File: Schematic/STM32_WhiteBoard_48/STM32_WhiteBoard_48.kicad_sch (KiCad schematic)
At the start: 41 parts, among them J1 SWDIO+Serial, J2 USB_B_Micro, J3 Header2, J4 Header1, SW1 BOOT0, SW2 RESET, U2 STM32F103CBTx, U3 LD3985M33R_SOT23, U3 W25Q32JVSSIQ, Y1 XC32M4-8.000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

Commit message: Minor layout changes
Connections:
- net PA10: now also J3.3 (Pin_3); no longer J3.4 (Pin_4)
- net PA11: now also J3.2 (Pin_2); no longer J3.3 (Pin_3)
- net PA12: now also J3.1 (Pin_1); no longer J3.2 (Pin_2)
- net PA15: now also J3.6 (Pin_6); no longer J3.1 (Pin_1)
- net PA8: now also J3.5 (Pin_5); no longer J3.6 (Pin_6)
- net PA9: now also J3.4 (Pin_4); no longer J3.5 (Pin_5)
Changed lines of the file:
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@@
     )
   )
-  (global_label "PA15" (shape bidirectional) (at 191.135 108.585 180) (fields_autoplaced)
-    (effects (font (size 1.27 1.27)) (justify right))
-    (property "Intersheetrefs" "${INTERSHEET_REFS}" (at 183.0739 108.585 0)
+  (global_label "PA15" (shape bidirectional) (at 191.135 121.285 180) (fields_autoplaced)
+    (effects (font (size 1.27 1.27)) (justify right))
+    (property "Intersheetrefs" "${INTERSHEET_REFS}" (at 183.0739 121.285 0)
       (effects (font (size 1.27 1.27)) (justify right) hide)
     )
@@
     )
   )
-  (global_label "PA8" (shape bidirectional) (at 191.135 121.285 180) (fields_autoplaced)
-    (effects (font (size 1.27 1.27)) (justify right))
-    (property "Intersheetrefs" "${INTERSHEET_REFS}" (at 184.2834 121.285 0)
+  (global_label "PA8" (shape bidirectional) (at 191.135 118.745 180) (fields_autoplaced)
+    (effects (font (size 1.27 1.27)) (justify right))
+    (property "Intersheetrefs" "${INTERSHEET_REFS}" (at 184.2834 118.745 0)
       (effects (font (size 1.27 1.27)) (justify right) hide)
     )
@@
     )
   )
-  (global_label "PA11" (shape bidirectional) (at 191.135 113.665 180) (fields_autoplaced)
-    (effects (font (size 1.27 1.27)) (justify right))
-    (property "Intersheetrefs" "${INTERSHEET_REFS}" (at 183.0739 113.665 0)
+  (global_label "PA11" (shape bidirectional) (at 191.135 111.125 180) (fields_autoplaced)
+    (effects (font (size 1.27 1.27)) (justify right))
+    (property "Intersheetrefs" "${INTERSHEET_REFS}" (at 183.0739 111.125 0)
       (effects (font (size 1.27 1.27)) (justify right) hide)
     )
@@
     )
   )
-  (global_label "PA12" (shape bidirectional) (at 191.135 111.125 180) (fields_autoplaced)
-    (effects (font (size 1.27 1.27)) (justify right))
-    (property "Intersheetrefs" "${INTERSHEET_REFS}" (at 183.0739 111.125 0)
+  (global_label "PA12" (shape bidirectional) (at 191.135 108.585 180) (fields_autoplaced)
+    (effects (font (size 1.27 1.27)) (justify right))
+    (property "Intersheetrefs" "${INTERSHEET_REFS}" (at 183.0739 108.585 0)
       (effects (font (size 1.27 1.27)) (justify right) hide)
     )
@@
     )
   )
-  (global_label "PA10" (shape bidirectional) (at 191.135 116.205 180) (fields_autoplaced)
-    (effects (font (size 1.27 1.27)) (justify right))
-    (property "Intersheetrefs" "${INTERSHEET_REFS}" (at 183.0739 116.205 0)
+  (global_label "PA10" (shape bidirectional) (at 191.135 113.665 180) (fields_autoplaced)
+    (effects (font (size 1.27 1.27)) (justify right))
+    (property "Intersheetrefs" "${INTERSHEET_REFS}" (at 183.0739 113.665 0)
       (effects (font (size 1.27 1.27)) (justify right) hide)
     )
@@
     )
   )
-  (global_label "PA9" (shape bidirectional) (at 191.135 118.745 180) (fields_autoplaced)
-    (effects (font (size 1.27 1.27)) (justify right))
-    (property "Intersheetrefs" "${INTERSHEET_REFS}" (at 184.2834 118.745 0)
+  (global_label "PA9" (shape bidirectional) (at 191.135 116.205 180) (fields_autoplaced)
+    (effects (font (size 1.27 1.27)) (justify right))
+    (property "Intersheetrefs" "${INTERSHEET_REFS}" (at 184.2834 116.205 0)
       (effects (font (size 1.27 1.27)) (justify right) hide)
     )
@@
         )
       )
+    )
+  )
+  (symbol (lib_id "power:PWR_FLAG") (at 53.975 165.1 0) (unit 1)
+    (in_bom yes) (on_board yes) (dnp no) (fields_autoplaced)
+    (property "Reference" "#FLG05" (at 53.975 163.195 0)
+      (effects (font (size 1.27 1.27)) hide)
+    )
+    (property "Value" "PWR_FLAG" (at 53.975 160.655 0)
+      (effects (font (size 1.27 1.27)) hide)
+    )
+    (property "Footprint" "" (at 53.975 165.1 0)
+      (effects (font (size 1.27 1.27)) hide)
+    )
+    (property "Datasheet" "~" (at 53.975 165.1 0)
+      (effects (font (size 1.27 1.27)) hide)
+    )
+    (pin "1")
+    (instances
+      (project "STM32_WhiteBoard_64"
+        (path "/b9086175-f44c-4e71-b882-25cd78abf8b0"
+          (reference "#FLG05") (unit 1)
+        )
+      )
+      (project "STM32_WhiteBoard_48"
+        (path "/e667a7e9-e434-40bf-934b-fbf6b9624752"
+          (reference "#FLG04") (unit 1)
+        )
+      )

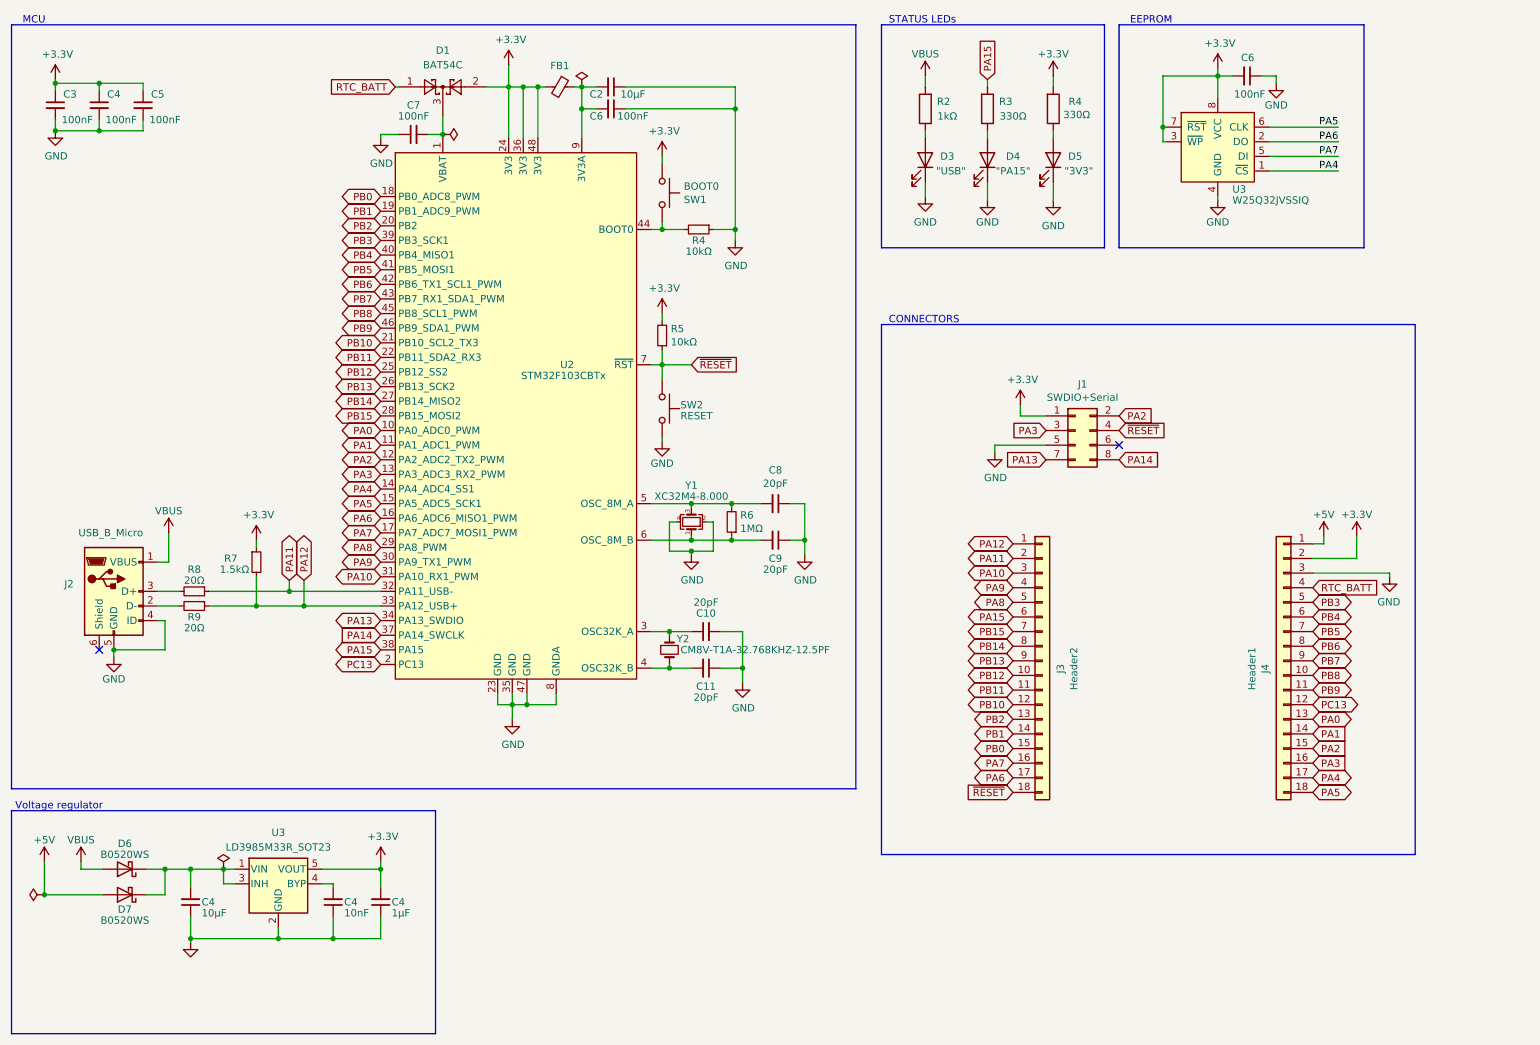
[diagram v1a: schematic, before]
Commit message: Added ESD protection for USB.
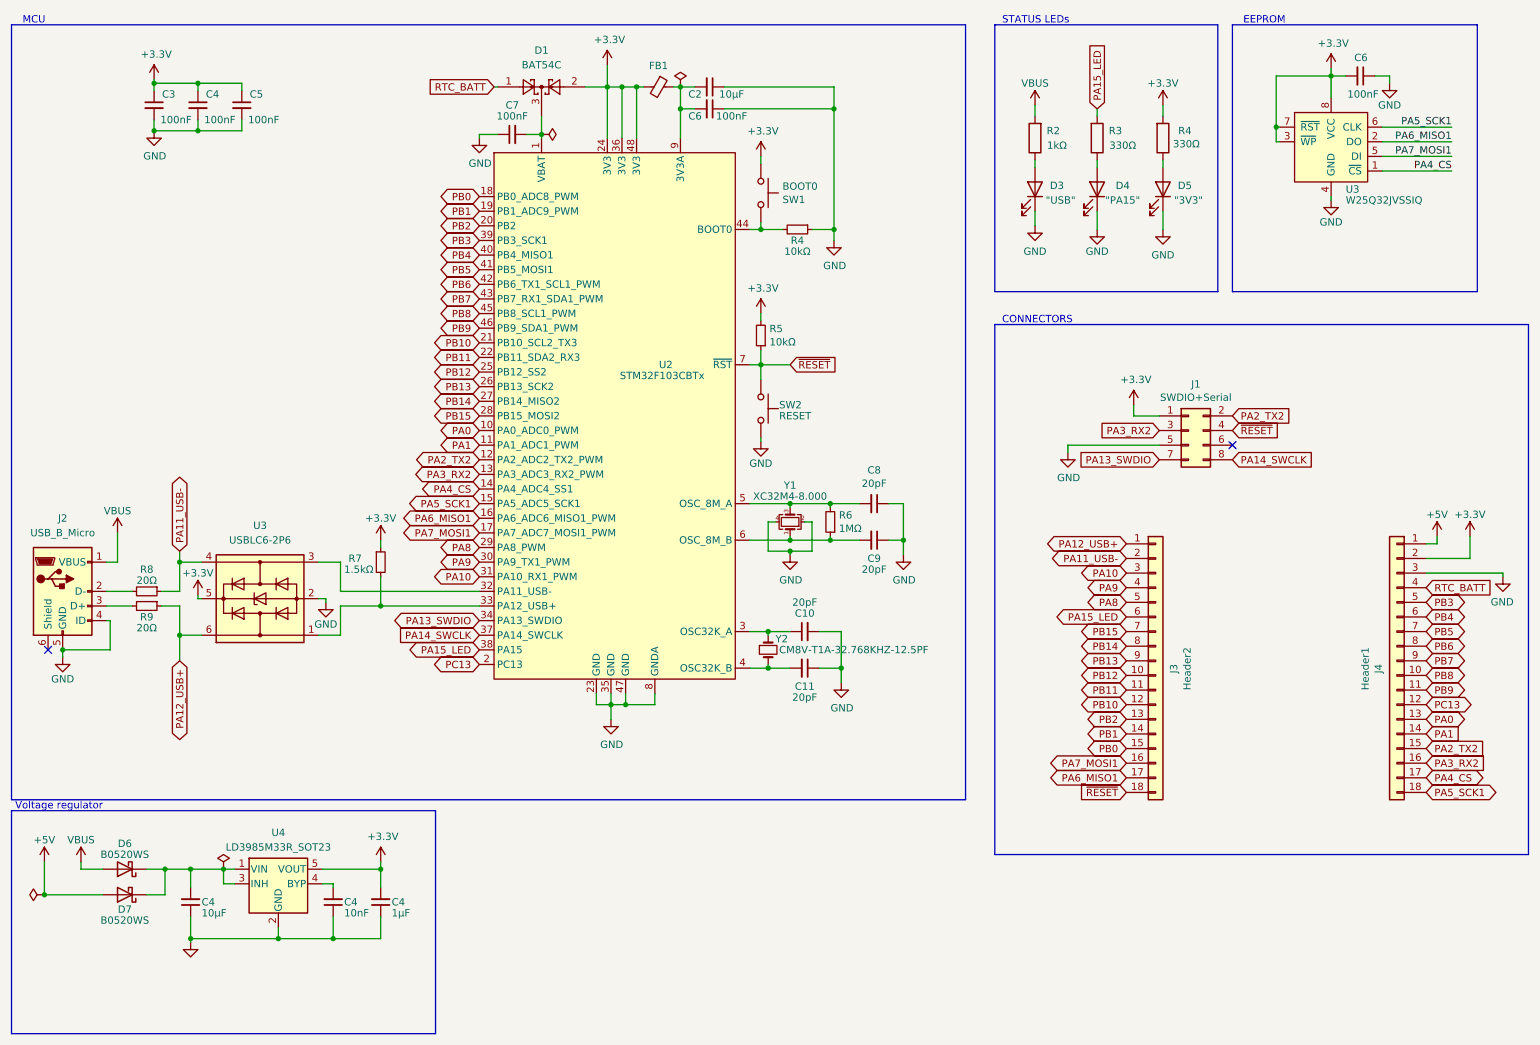
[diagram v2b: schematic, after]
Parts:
- removed J2: USB_B_Micro, digikey-footprints:USB_Micro_B_Female_10118194-0001LF, symbol Connector:USB_B_Micro
- added J2: USB_B_Micro, Retronics_Connectors:USB_Micro_B_Female_10118194-0001LF, symbol Retronics_Connectors:USB_B_Micro
- added U3: USBLC6-2P6, Retronics_IC:USBLC6-2SC6, symbol Retronics_Integrated_Circuits:USBLC6-2P6
- renumbered U3 to U4
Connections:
- net +3.3V: now also U3.5 (VBUS)
- net GND: now also J2.4 (ID), J2.5 (GND), U3.2 (GND)
- net VBUS: now also J2.1 (VBUS)
- net at R8.2: now also J2.2 (D-)
- net at R9.2: now also J2.3 (D+)
- net PA11 renamed PA11_USB-
- net PA11_USB-: now also U3.4 (I/O2); no longer U2.32 (PA11_USB-)
- net PA12: no longer names the net of R7.2, U2.33 (PA12_USB+)
- net PA12: now also U3.1 (I/O1); no longer J3.1 (Pin_1), R9.1
- net PA13 renamed PA13_SWDIO
- net PA14 renamed PA14_SWCLK
- net PA15 renamed PA15_LED
- net PA2 renamed PA2_TX2
- net PA3 renamed PA3_RX2
- net PA4 renamed PA4_CS
- net PA5 renamed PA5_SCK1
- net PA6 renamed PA6_MISO1
- net PA7 renamed PA7_MOSI1
- new net: U2.32 (PA11_USB-), U3.3 (I/O2)
- new net PA12_USB+: J3.1 (Pin_1), R9.1, U3.6 (I/O1)
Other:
- moved on the sheet: C10, C11, C2, C3, C4, C5, C6, C7, C8, C9, D1, D3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
